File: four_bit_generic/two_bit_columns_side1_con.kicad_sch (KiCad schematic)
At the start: 2 parts

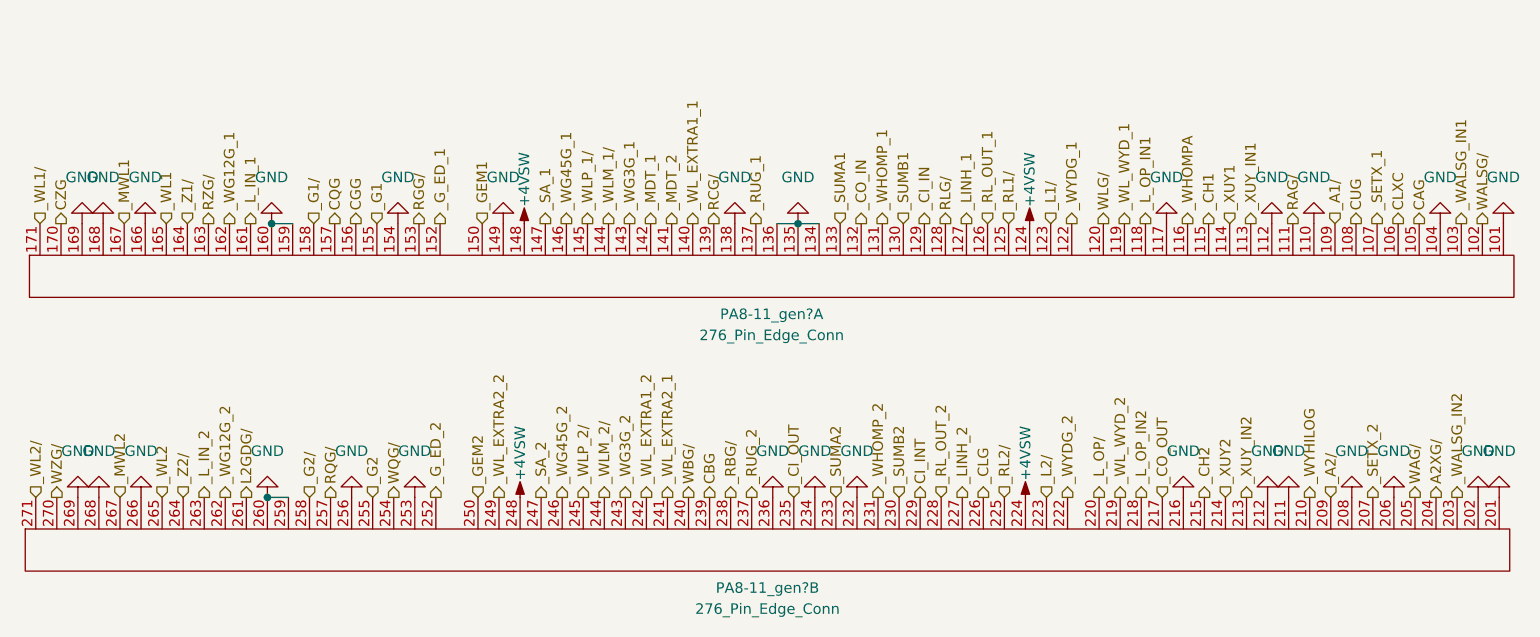
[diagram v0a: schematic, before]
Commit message: Generic  4 Bit Adder schematic + pcb
PCB and schematic updates
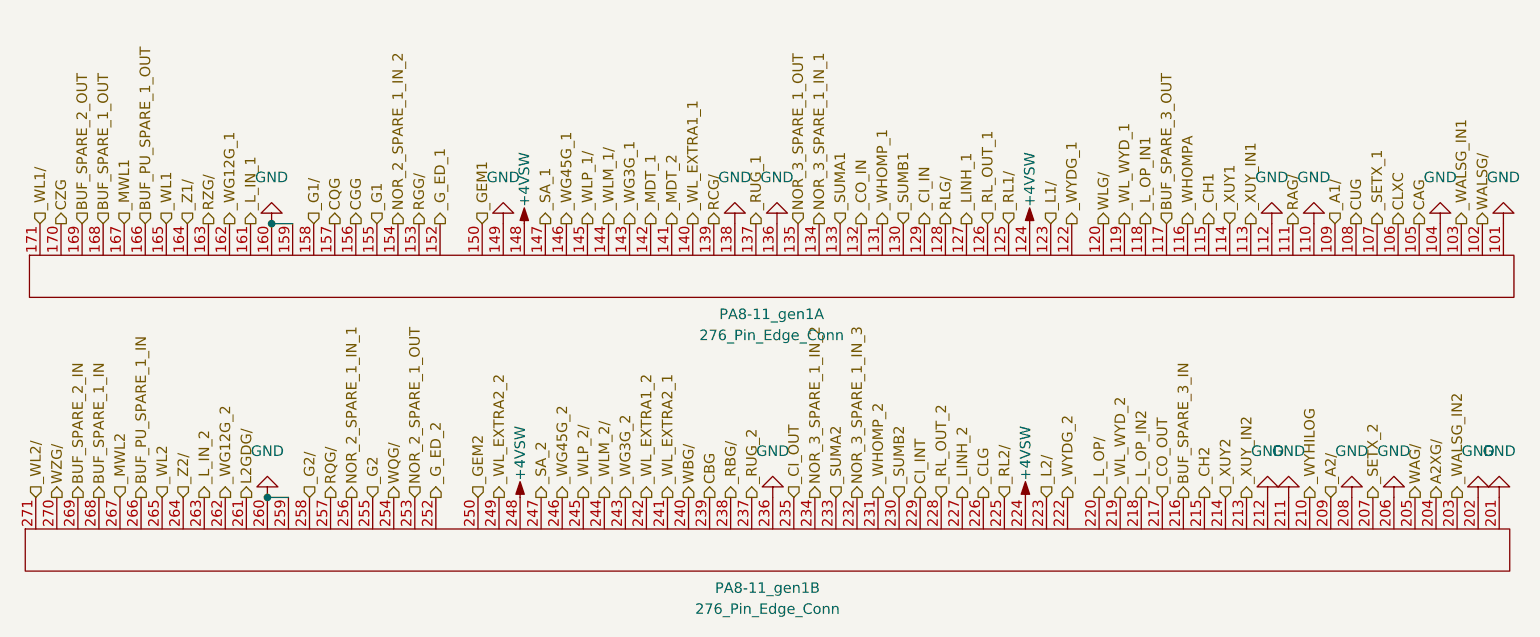
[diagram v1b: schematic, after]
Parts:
- gave numbers to parts that had none: 1
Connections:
- net GND: no longer PA8-11_gen1.117, PA8-11_gen1.134, PA8-11_gen1.135, PA8-11_gen1.154, PA8-11_gen1.166, PA8-11_gen1.168, PA8-11_gen1.169, PA8-11_gen1.216, PA8-11_gen1.232, PA8-11_gen1.234, PA8-11_gen1.253, PA8-11_gen1.256, PA8-11_gen1.266, PA8-11_gen1.268, PA8-11_gen1.269
- new net BUF_PU_SPARE_1_IN: PA8-11_gen1.266
- new net BUF_PU_SPARE_1_OUT: PA8-11_gen1.166
- new net BUF_SPARE_1_IN: PA8-11_gen1.268
- new net BUF_SPARE_1_OUT: PA8-11_gen1.168
- new net BUF_SPARE_2_IN: PA8-11_gen1.269
- new net BUF_SPARE_2_OUT: PA8-11_gen1.169
- new net BUF_SPARE_3_IN: PA8-11_gen1.216
- new net BUF_SPARE_3_OUT: PA8-11_gen1.117
- new net NOR_2_SPARE_1_IN_1: PA8-11_gen1.256
- new net NOR_2_SPARE_1_IN_2: PA8-11_gen1.154
- new net NOR_2_SPARE_1_OUT: PA8-11_gen1.253
- new net NOR_3_SPARE_1_IN_1: PA8-11_gen1.134
- new net NOR_3_SPARE_1_IN_2: PA8-11_gen1.234
- new net NOR_3_SPARE_1_IN_3: PA8-11_gen1.232
- new net NOR_3_SPARE_1_OUT: PA8-11_gen1.135
